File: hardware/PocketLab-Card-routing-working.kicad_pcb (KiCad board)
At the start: 4 copper layers, 85.6 x 54 mm, 260 parts, among them J1 USB-C DATA/POWER, J2 microSD, J3 EXTERNAL 400uH LF COIL, J4 PROTECTED 1S LiPo 3.7V, J5 30-PIN 2.54mm DUPONT GRID, Q1 AO3400A IR DRIVER, Q2 CSD16406Q3 DISCHARGE, Q3 CSD16406Q3 CHARGE, SW1 RESET, SW2 BOOT, SW3 UP, SW4 DOWN, SW5 MAIN POWER OFF / ON, SW6 PAIR, SW7 SELECT, SW8 AUX CONFIG, U1 ESP32-S3-WROOM-1-N8R2, U10 BMI270 (FULL OPTION), U11 BMP390 (FULL OPTION), U12 PCF8563T, U13 TSOP75338WTR 38kHz, U14 BQ29700DSE, U15 TPS2553DBVR 500mA LIMIT, U16 USBLC6-4SC6Y, U17 TPS22919DCKR LF 5V LOAD SWITCH, U18 TCA9534PWR INTERNAL CONTROL, U19 SRV05-4MR6T1G SD ESD, U2 PN5321A3HN/C106, U20 SN74AHCT1G126DBVR RGB LEVEL S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, U21 SN74LV125ATPWR LF/SPI 3V3-TO-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, U22 SN74LVC1G126DBVR LF 5V-TO-3V3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, U23 ATECC608C-SSHDA-T, U24 SRV05-4MR6T1G J5 BUS ESD, U25 SRV05-4MR6T1G J5 SPI ESD, U3 E07-900MM10S 855-925MHz, U4 HTRC11001T/03EE,11 125kHz, U5 BQ24074RGTR, U6 TPS63070RNMR 3V3, U7 TPS61023DRLR 5V BOOST, U8 MAX17048G+T10, U9 TCA9535PWR, Y301 27.12MHz crystal (pins 2/4 sh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, Y501 4MHz 5V CMOS OSCILLATOR, Y701 32.768kHz CL=7pF

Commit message: Reroute user button conflict corridor
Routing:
- net /USER_BUTTON_A_N: track 47.6 -> 48.2 mm
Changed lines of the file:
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@@
 	(segment
 		(start 68.6 38.35)
+		(end 69.6 36.75)
+		(width 0.15)
+		(locked yes)
+		(layer "In1.Cu")
+		(net "/USER_BUTTON_A_N")
+	)
+	(segment
+		(start 69.6 36.75)
+		(end 70.199999 31.75)
+		(width 0.15)
+		(locked yes)
+		(layer "In1.Cu")
+		(net "/USER_BUTTON_A_N")
+	)
+	(segment
+		(start 70.199999 31.75)
+		(end 71.6 30.75)
+		(width 0.15)
+		(locked yes)
+		(layer "In1.Cu")
+		(net "/USER_BUTTON_A_N")
+	)
+	(segment
+		(start 71.6 30.75)
 		(end 72.1375 30.475)
 		(width 0.15)

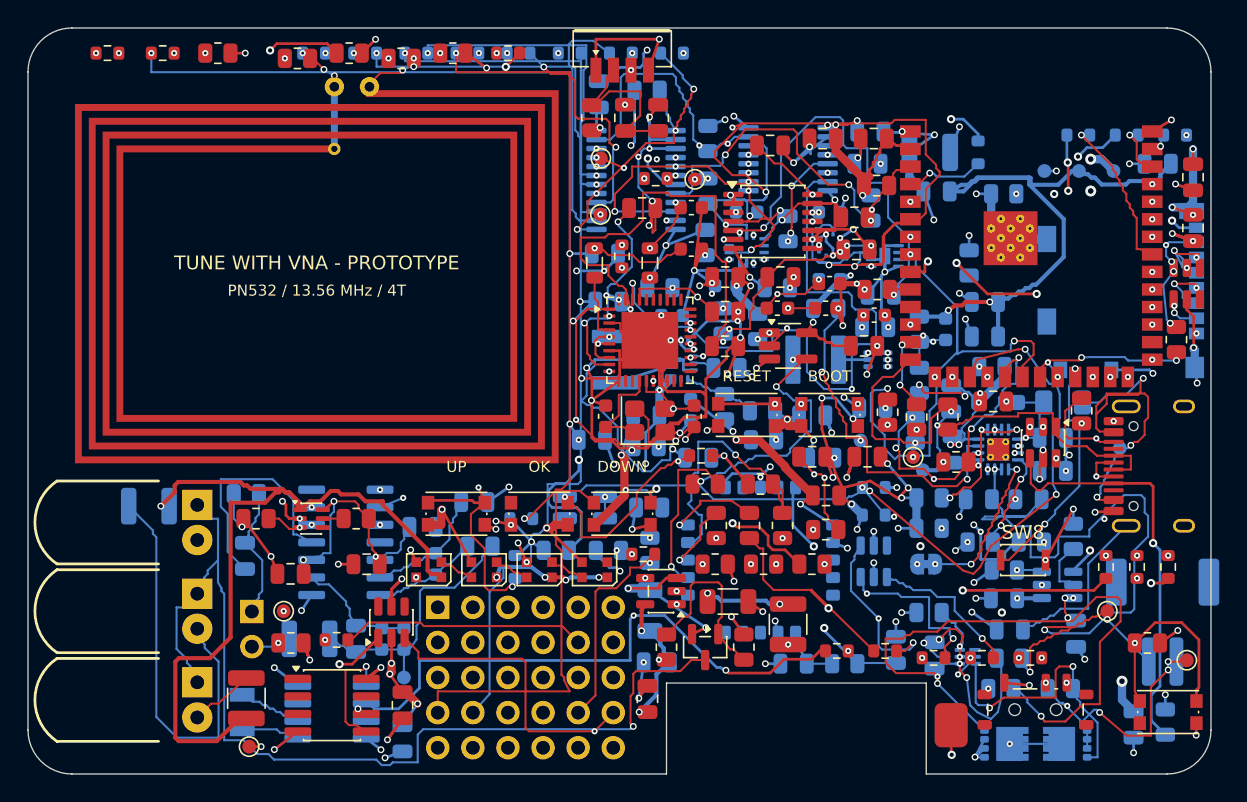
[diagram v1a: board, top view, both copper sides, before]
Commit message: Refine congested routing corridors
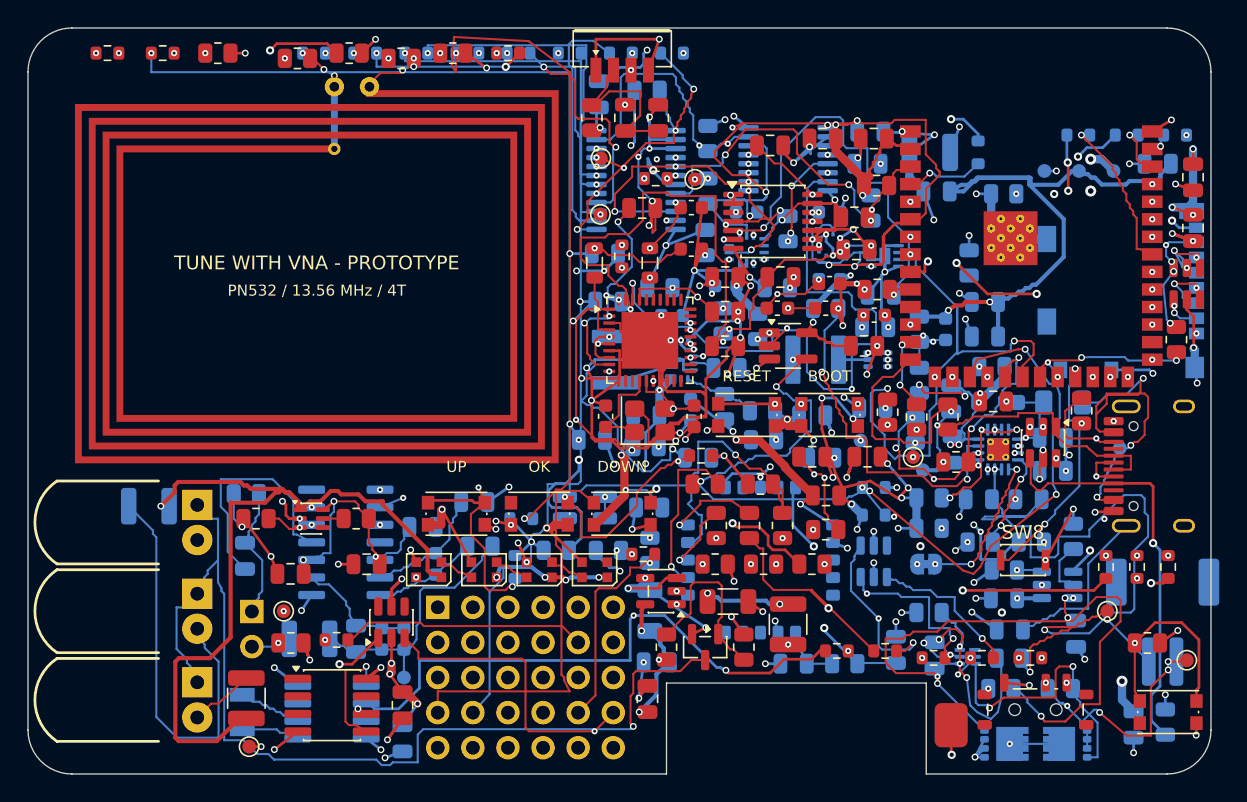
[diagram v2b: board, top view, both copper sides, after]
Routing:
- net /GPIO8_MCU: track 100.8 -> 109.6 mm
- net /EX4: track 66.5 -> 70.0 mm
- net /SD_DETECT_N: track 64.1 -> 66.5 mm
- net /AUX5_FAULT_N: track 75.0 -> 76.9 mm
- net /CHG_TS_FIXED: track 33.5 -> 35.1 mm
- net /BAT_SENSE: track 19.3 -> 20.7 mm
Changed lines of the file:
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@@
 	(segment
 		(start 59.2 52.8)
+		(end 59.2 41.46)
+		(width 0.15)
+		(locked yes)
+		(layer "In2.Cu")
+		(net "/GPIO8_MCU")
+	)
+	(segment
+		(start 59.2 41.46)
 		(end 83.85 41.46)
 		(width 0.15)
@@
 	(segment
 		(start 93.8 44.2)
+		(end 93.8 45.7)
+		(width 0.15)
+		(locked yes)
+		(layer "In2.Cu")
+		(net "/SD_DETECT_N")
+	)
+	(segment
+		(start 93.8 45.7)
+		(end 66.8625 45.7)
+		(width 0.15)
+		(locked yes)
+		(layer "In2.Cu")
+		(net "/SD_DETECT_N")
+	)
+	(segment
+		(start 66.8625 45.7)
 		(end 66.8625 44.74)
 		(width 0.15)
@@
 	(segment
 		(start 50.975 23.2)
+		(end 50.675 22.75)
+		(width 0.15)
+		(locked yes)
+		(layer "F.Cu")
+		(net "/EX4")
+	)
+	(segment
+		(start 50.675 22.75)
+		(end 50.825 20.65)
+		(width 0.15)
+		(locked yes)
+		(layer "F.Cu")
+		(net "/EX4")
+	)
+	(segment
+		(start 50.825 20.65)
+		(end 56.225 20.95)
+		(width 0.15)
+		(locked yes)
+		(layer "F.Cu")
+		(net "/EX4")
+	)
+	(segment
+		(start 56.225 20.95)
 		(end 59.2 23.2)
 		(width 0.15)
@@
 		(net "/AUX5_FAULT_N")
 	)
+	(segment
+		(start 64.8524 29.4448)
+		(end 65.25 30.3)
+		(width 0.2)
+		(layer "B.Cu")
+		(locked yes)
+		(net "/AUX5_FAULT_N")
+	)
+	(segment
+		(start 64.8524 29.4448)
+		(end 65.25 30.3)
+		(width 0.2)
+		(layer "In2.Cu")
+		(locked yes)
+		(net "/AUX5_FAULT_N")
+	)
 	(via
-		(at 64.8524 29.4448)
+		(at 65.25 30.3)
 		(size 0.6)
 		(drill 0.3)
@@
 		(net "/BAT_SENSE")
 	)
+	(segment
+		(start 87.425 65.5)
+		(end 86.75 65.35)
+		(width 0.15)
+		(layer "B.Cu")
+		(locked yes)
+		(net "/BAT_SENSE")
+	)
+	(segment
+		(start 87.425 65.5)
+		(end 86.75 65.35)
+		(width 0.15)
+		(layer "In2.Cu")
+		(locked yes)
+		(net "/BAT_SENSE")
+	)
 	(via
-		(at 87.425 65.5)
+		(at 86.75 65.35)
 		(size 0.45)
 		(drill 0.2)
@@
 		(width 0.15)
 		(locked yes)
-		(layer "In1.Cu")
+		(layer "In2.Cu")
 		(net "/CHARGER_CHG_N")
 	)
@@
 	(segment
 		(start 75.4 38.795)
+		(end 76.2 38.795)
+		(width 0.15)
+		(locked yes)
+		(layer "In1.Cu")
+		(net "/CHG_TS_FIXED")
+	)
+	(segment
+		(start 76.2 38.795)
+		(end 76.2 60)
+		(width 0.15)
+		(locked yes)
+		(layer "In1.Cu")
+		(net "/CHG_TS_FIXED")
+	)
+	(segment
+		(start 76.2 60)
 		(end 75.4 60)
 		(width 0.15)
